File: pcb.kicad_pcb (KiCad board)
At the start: 2 copper layers, 51.2 x 73 mm, 48 parts, among them J1 USB_B_Mini, J2 Conn_ARM_JTAG_SWD_20, J3 Micro_SD_Card_Det1, J4 Conn_02x25_Odd_Even, J5 Conn_02x25_Odd_Even, SW1 SW_RESET, U1 STM32H750VBTx, U2 USBLC6-2P6, U3 TLV1117-33, Y2 25MHz 9pF

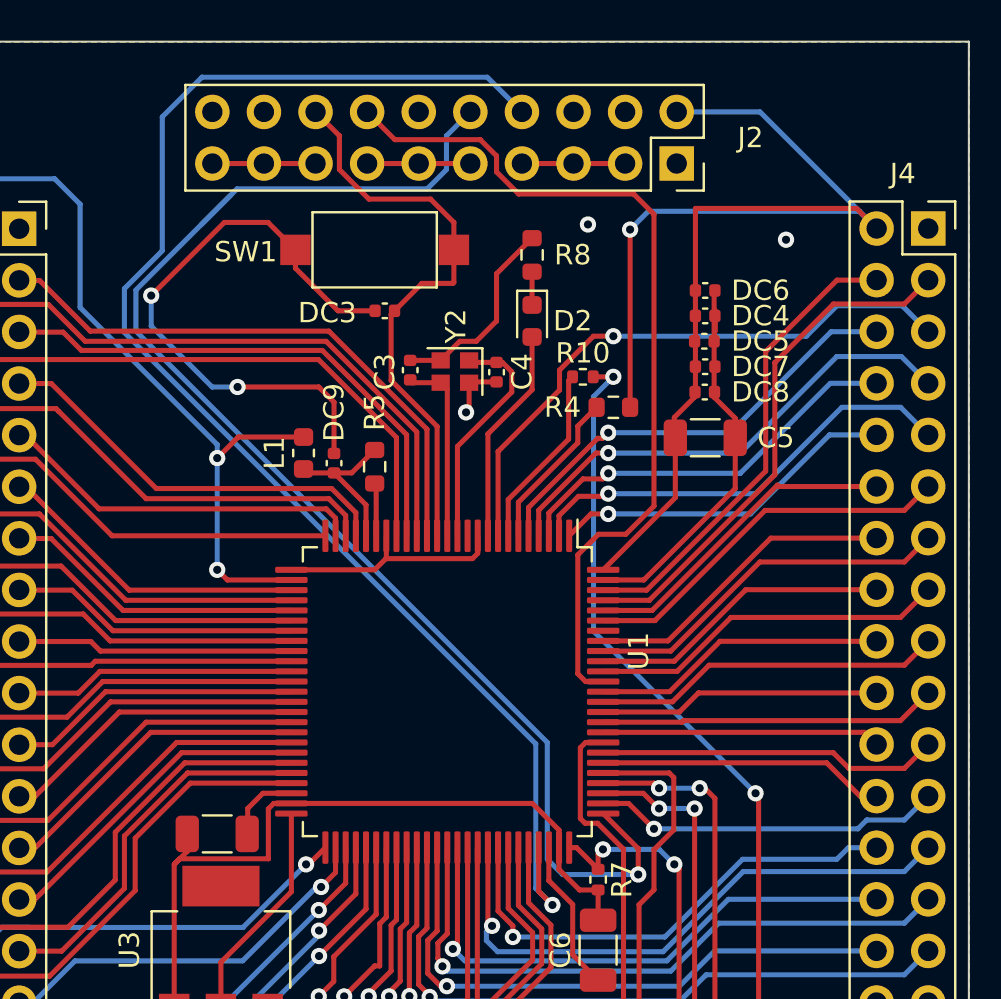
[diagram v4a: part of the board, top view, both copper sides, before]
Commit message: BOM: Updates BOM to remove out of stock parts, switched out reset switch, new footprint SPST-NO 3.5x6.0mm, moved it away from connector due to it's higher profile
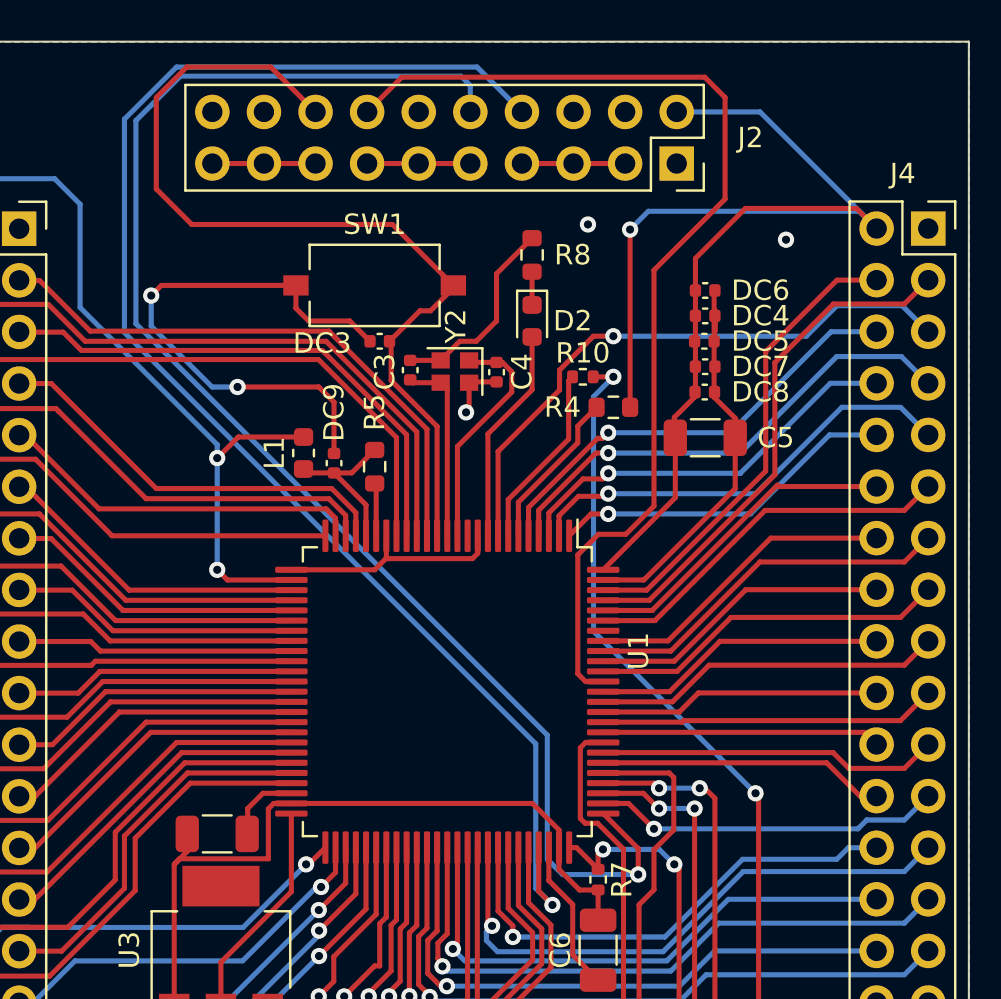
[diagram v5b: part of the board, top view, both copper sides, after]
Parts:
- SW1: footprint Button_Switch_SMD:SW_SPST_CK_RS282G05A3 -> Button_Switch_SMD:SW_Tactile_SPST_NO_Straight_CK_PTS636Sx25SMTRLFS
- moved SW1 1.75 mm to (82.8, 57.0)
- moved DC3 1.52 mm to (83.0, 59.8)
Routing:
- net RESET: track 28.6 -> 45.8 mm
- net PB3: track 43.0 -> 52.3 mm
- net PA14: track 68.0 -> 72.1 mm
- net Earth: track 242.0 -> 240.0 mm
- net BOOT0: track 198.4 -> 197.0 mm
- net PA13: track 70.6 -> 72.1 mm
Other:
- board text added: "10-Year Anniversary - I love you v1.3"
- board text removed: "10-Year Anniversary v1.2"

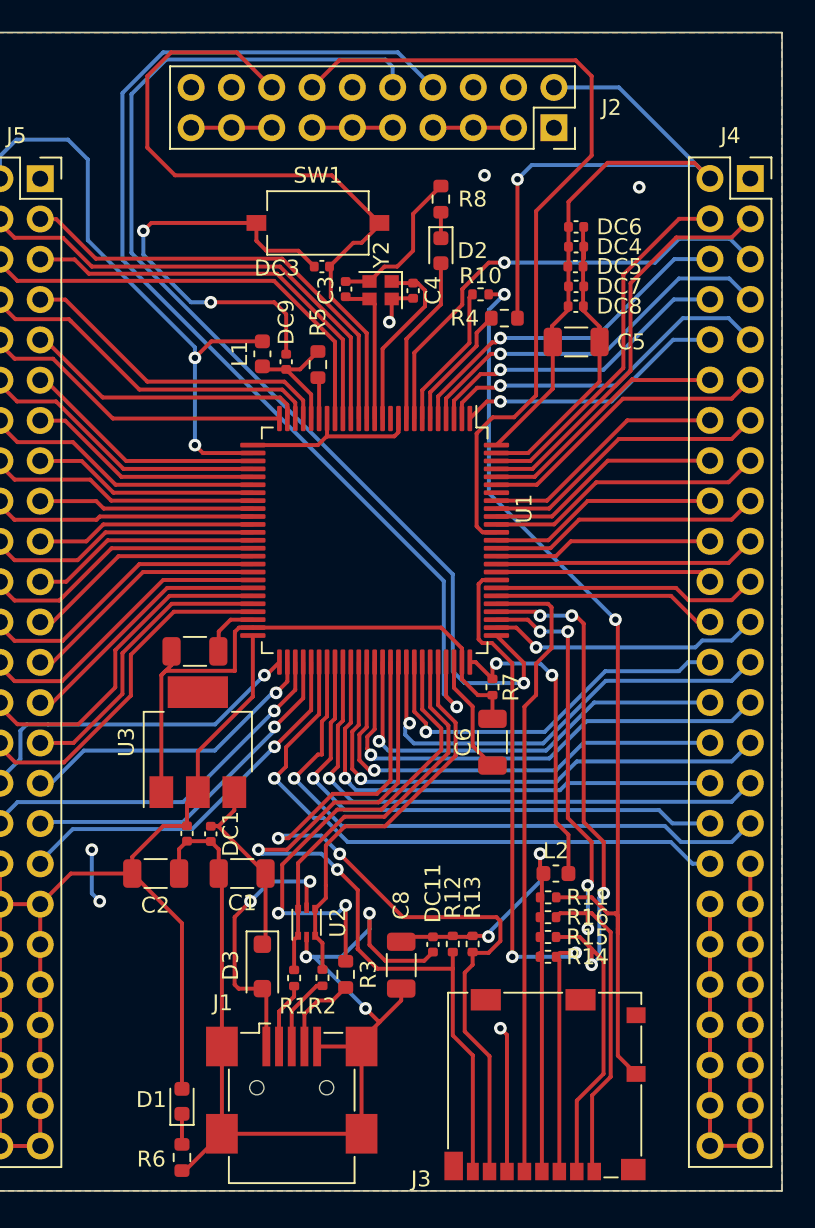
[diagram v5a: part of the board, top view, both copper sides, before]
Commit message: PCB: Fixed clearance violations
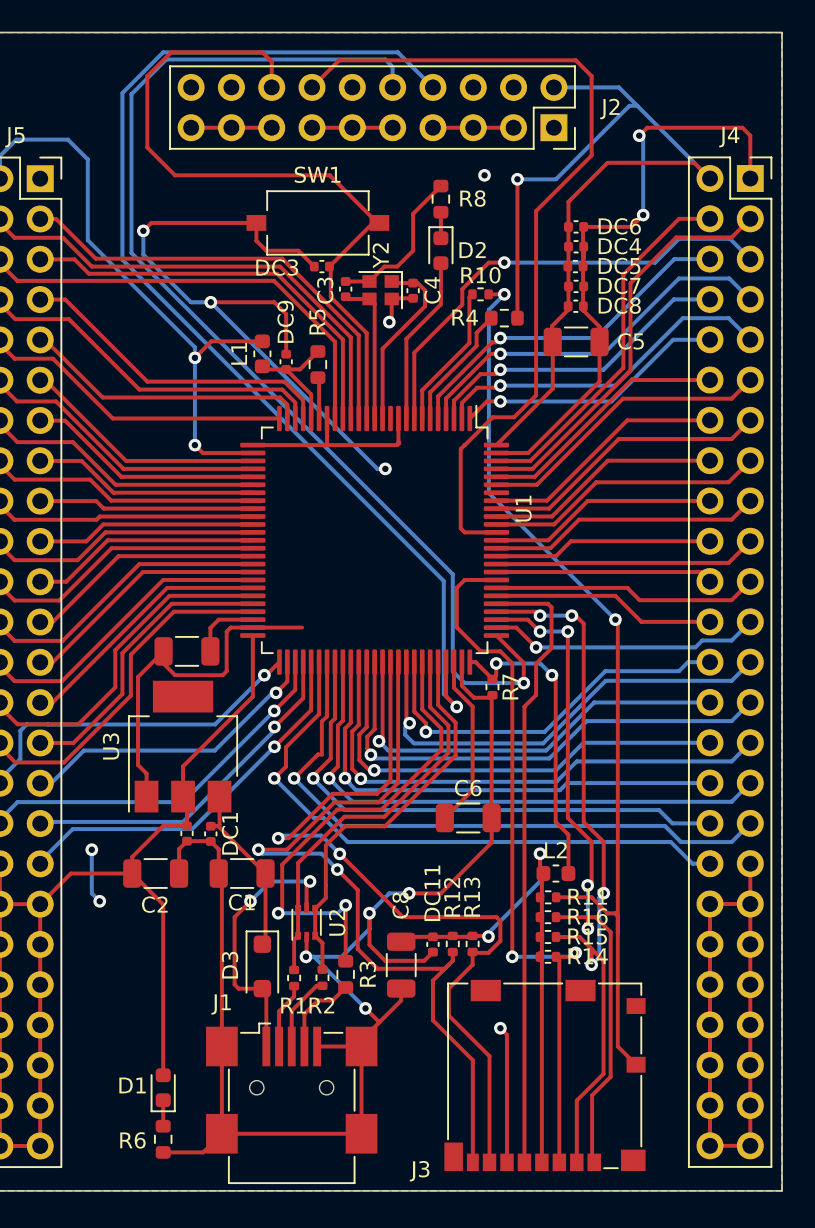
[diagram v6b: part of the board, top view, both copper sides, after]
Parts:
- moved C6 5.01 mm to (92.2, 94.5), turned to 0 degrees
- moved R6 1.65 mm to (73.0, 114.8)
- moved D1 1.46 mm to (73.0, 111.5)
- moved U3 0.97 mm to (74.2, 90.0)
- moved J3 0.58 mm to (97.1, 110.8)
- moved C7 0.50 mm to (74.5, 84.0)
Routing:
- net Earth: track 240.0 -> 287.7 mm, vias 11 -> 14
- net BOOT0: track 197.0 -> 192.4 mm
- net Net-(C6-Pad1): track 7.53 -> 11.0 mm
- net PD2: track 45.0 -> 46.6 mm
- net PB3: track 52.3 -> 53.8 mm
- net Net-(J3-DAT2): track 44.9 -> 43.9 mm
- net +5V: track 11.8 -> 11.1 mm
- net Net-(C7-Pad1): track 3.72 -> 4.37 mm
- net Net-(J3-VDD): track 33.2 -> 32.7 mm
- net Net-(J3-DET): track 59.8 -> 59.2 mm
- net Net-(J3-DAT3/CD): track 46.9 -> 46.3 mm
- net Net-(J3-CLK): track 39.8 -> 39.3 mm
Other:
- board text added: "10 Year Anniversary - I love you v1.3"
- board text removed: "10-Year Anniversary - I love you v1.3"
